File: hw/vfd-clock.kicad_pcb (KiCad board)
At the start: 2 copper layers, 150 x 50 mm, 47 parts, among them CON1 BARREL_JACK_2, CON2 BARREL_JACK_2, M1 MountingHole_4-5mm, M2 MountingHole_4-5mm, P1 ST_LINK, P2 GPS, Q1 PNP, Q2 PNP, SW1 SET, SW2 UP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

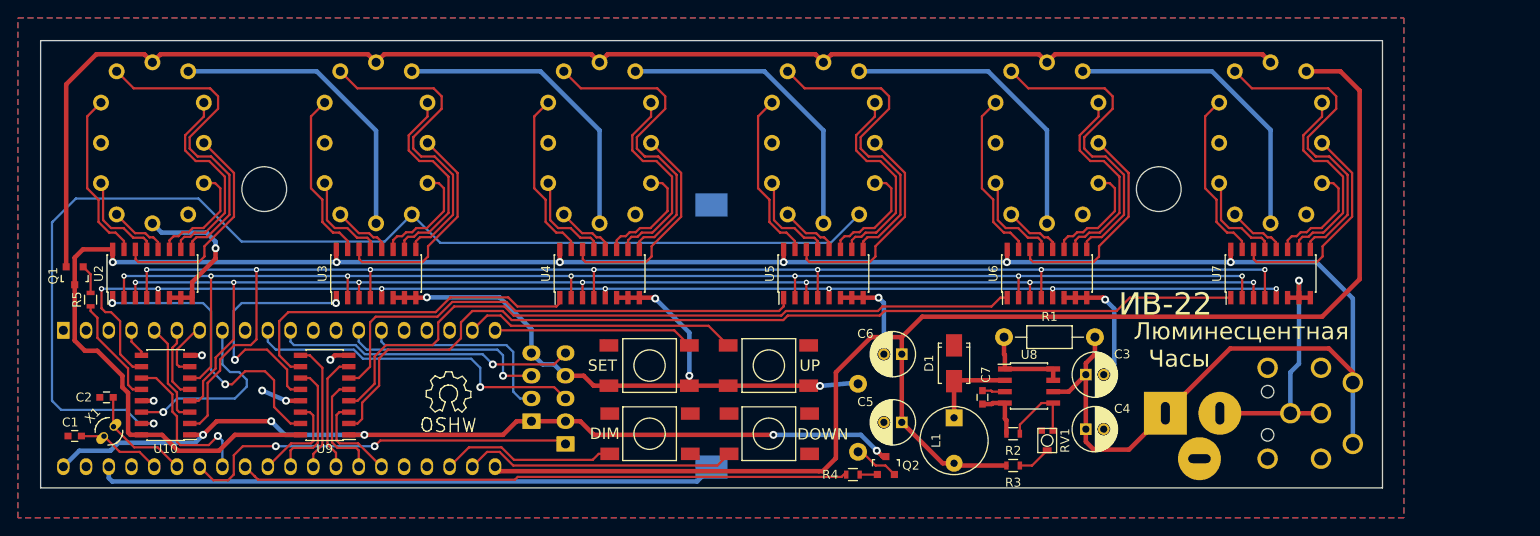
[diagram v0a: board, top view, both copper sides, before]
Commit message: fix transistor pin orientation
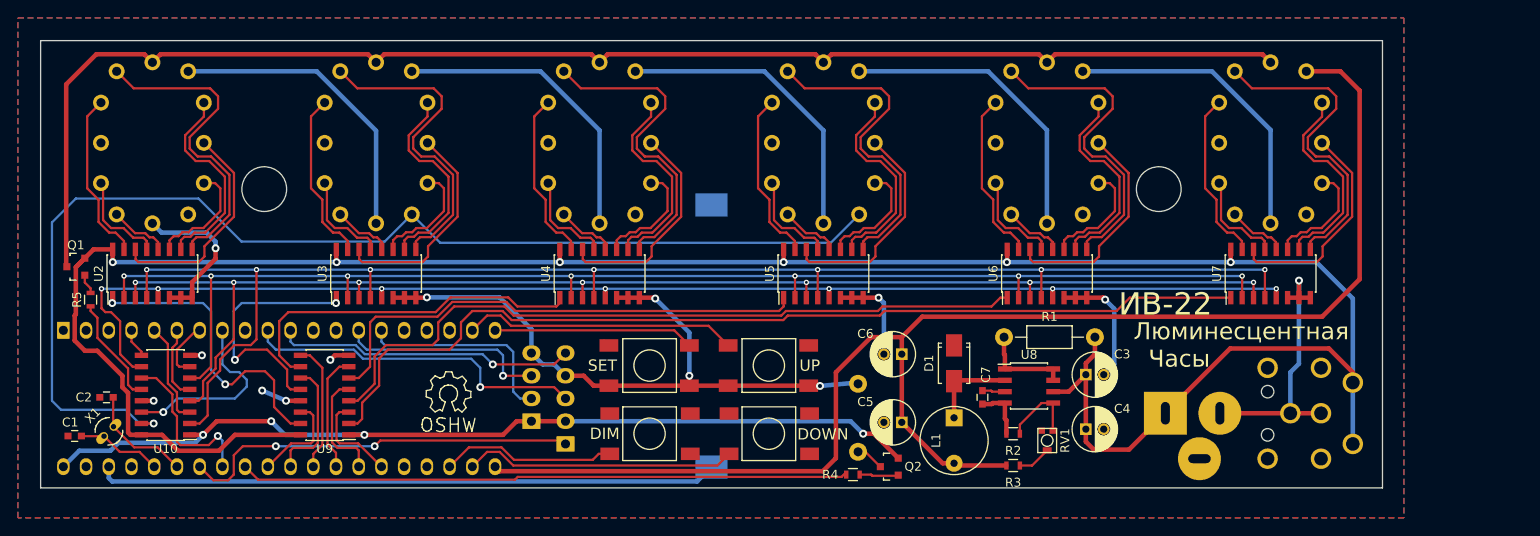
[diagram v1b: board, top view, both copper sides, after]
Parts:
- moved Q1 1.02 mm to (29.3, 50.7), turned to 90 degrees
- moved Q2 0.40 mm to (120.3, 73.0), turned to 90 degrees
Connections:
- Q1 pad 1: /GRID -> /19v5
- Q1 pad 3: /19v5 -> /GRID
- Q2 pad 1: Net-(Q2-Pad1) -> /3v3
- Q2 pad 3: /3v3 -> Net-(Q2-Pad3)
- SP1 pad 1: Net-(Q2-Pad1) -> Net-(Q2-Pad3)
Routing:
- net Net-(Q2-Pad1): track 5.04 -> 0.00 mm
- net Net-(Q2-Pad3): track 0.00 -> 3.18 mm
- net Net-(Q2-Pad2): track 1.99 -> 4.39 mm
- net /3v3: track 100.2 -> 101.6 mm, vias 5 -> 4
- net Net-(Q1-Pad2): track 3.26 -> 2.25 mm
- net /19v5: track 268.5 -> 269.3 mm

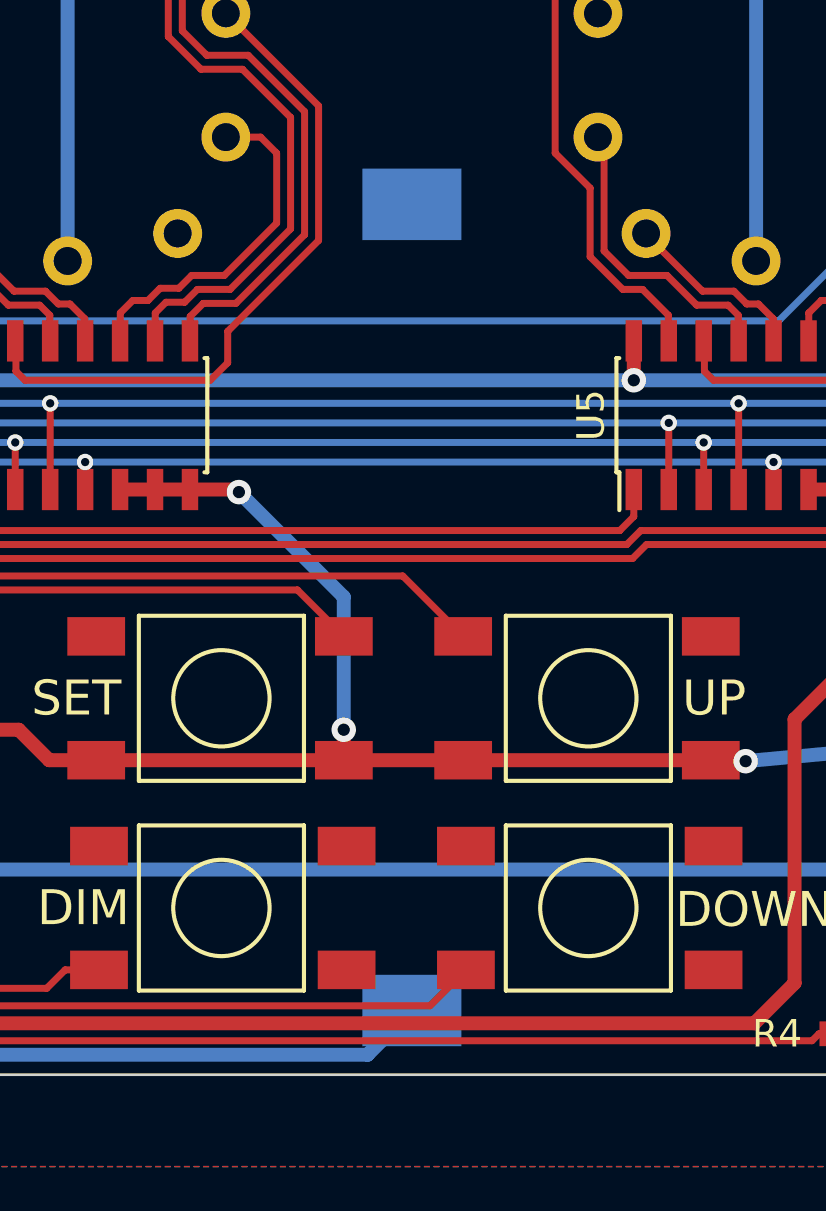
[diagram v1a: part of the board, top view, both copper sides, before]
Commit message: widen battery terminals for easier hand soldering
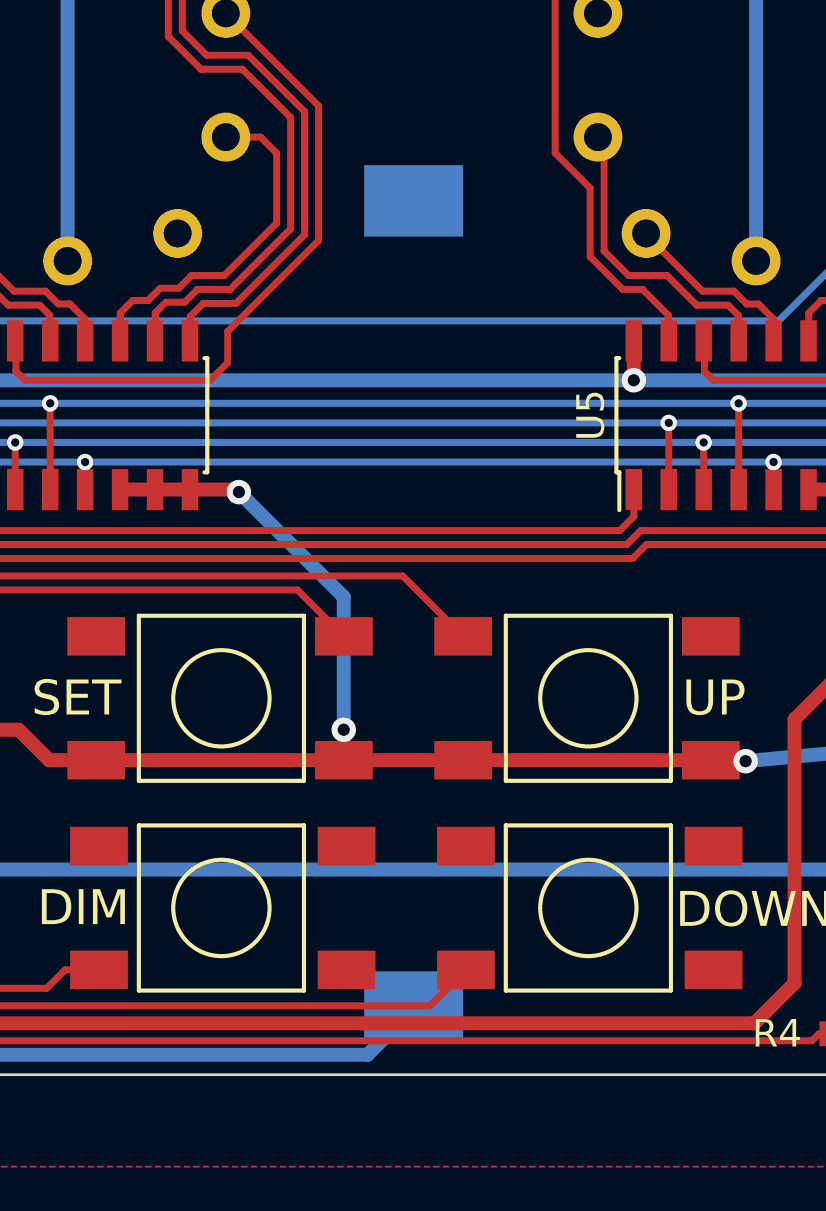
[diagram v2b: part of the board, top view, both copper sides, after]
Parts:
- moved BT1 0.14 mm to (100.5, 58.3)

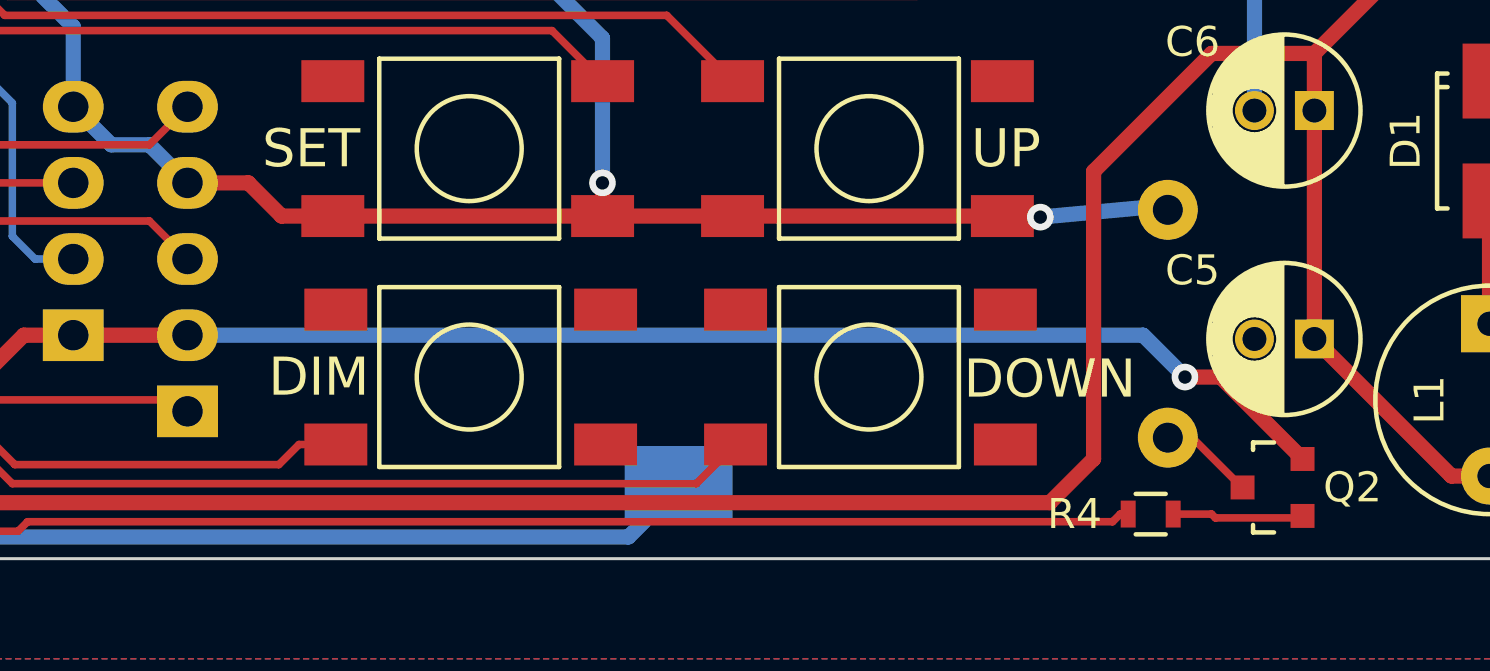
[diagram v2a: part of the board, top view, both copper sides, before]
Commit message: fix buzzer pin width
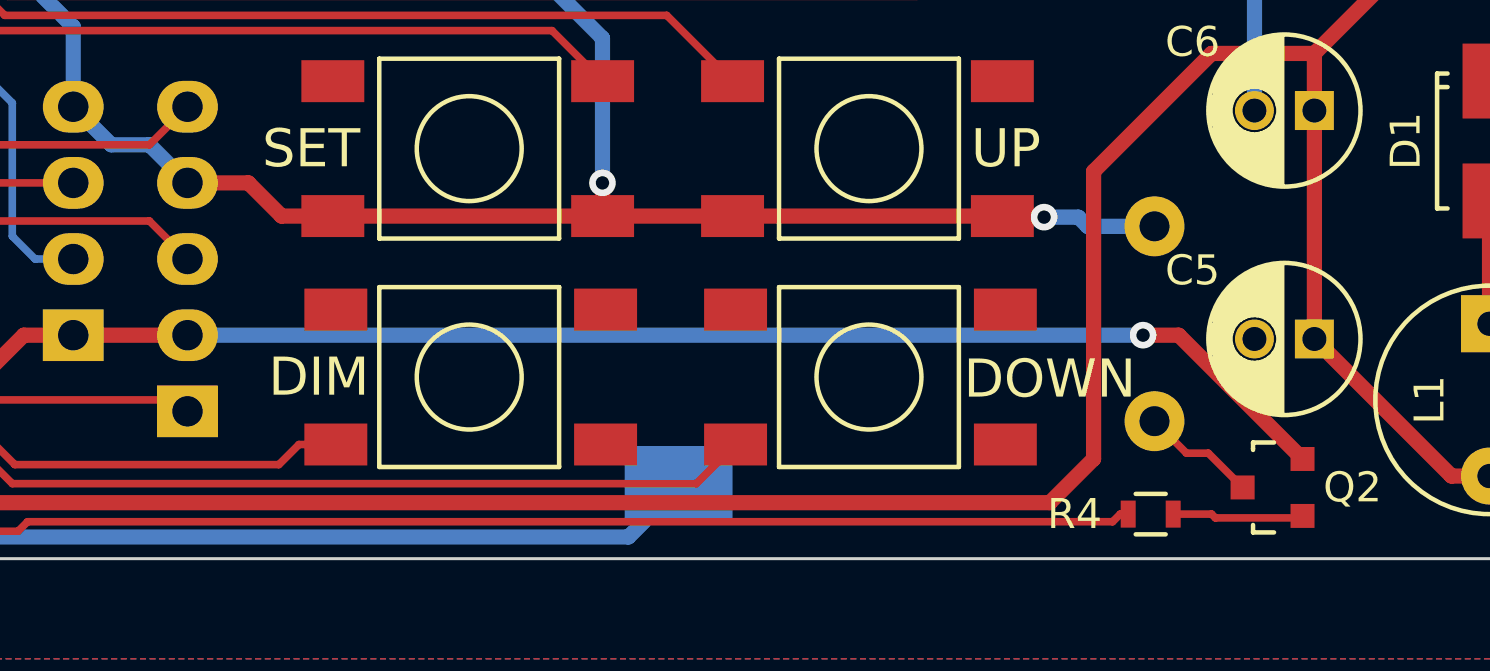
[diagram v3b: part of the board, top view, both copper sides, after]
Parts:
- SP1: footprint Buzzers_Beepers:Buzzer_12x9.5RM7.6 -> AT-1224-TWT
- moved SP1 0.44 mm to (116.3, 67.6)
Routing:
- net Net-(Q2-Pad3): track 3.18 -> 3.87 mm
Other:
- rule trace_min: 0.254 -> 0.01
- rule via_min_size: 0.381 -> 0.015
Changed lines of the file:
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@@
     (thickness 1.6)
     (drawings 11)
-    (tracks 1039)
+    (tracks 1041)
     (zones 0)
     (modules 47)
@@
     (zone_clearance 0.254)
     (zone_45_only no)
-    (trace_min 0.254)
+    (trace_min 0.01)
     (segment_width 0.2)
     (edge_width 0.1)
     (via_size 0.889)
     (via_drill 0.635)
-    (via_min_size 0.381)
+    (via_min_size 0.015)
     (via_min_drill 0.254)
     (uvia_size 0.508)
     (uvia_drill 0.127)
     (uvias_allowed yes)
-    (uvia_min_size 0.508)
+    (uvia_min_size 0.02)
     (uvia_min_drill 0.127)
     (pcb_text_width 0.3)
@@
     (add_net "Net-(D1-Pad2)")
   )
+  (module AT-1224-TWT (layer B.Cu)
+    (at 116.332 67.564 90)
+    (descr "Generic Buzzer, D12mm height 9.5mm with RM7.6mm")
+    (tags buzzer)
+    (fp_text reference SP1 (at 0 6.985 90) (layer B.SilkS)
+      (effects (font (size 1 1) (thickness 0.15)) (justify mirror))
+    )
+    (fp_text value SPEAKER (at 0 -8.255 90) (layer B.Fab)
+      (effects (font (size 1 1) (thickness 0.15)) (justify mirror))
+    )
+    (fp_text user + (at -3.175 2.54 90) (layer B.SilkS)
+      (effects (font (size 1 1) (thickness 0.15)) (justify mirror))
+    )
+    (fp_circle (center 0 0) (end 6 0) (layer B.SilkS) (width 0.15))
+    (pad 1 thru_hole circle (at -3.25 0 90) (size 2 2) (drill 1.00076) (layers *.Cu *.Mask B.SilkS)
+      (net 97 "Net-(Q2-Pad3)"))
+    (pad 2 thru_hole circle (at 3.25 0 90) (size 2 2) (drill 1.00076) (layers *.Cu *.Mask B.SilkS)
+      (net 1 /GND))
+    (model Buzzers_Beepers.3dshapes/Buzzer_12x9.5RM7.6.wrl
+      (at (xyz 0 0 0))
+      (scale (xyz 4 4 4))
+      (rotate (xyz 0 0 0))
+    )
+  )
   (module Diodes_SMD:Diode-SMA_Standard (layer F.Cu)
     (at 127.508 61.468 270)
@@
     )
   )
-  (module Buzzers_Beepers:Buzzer_12x9.5RM7.6 (layer B.Cu)
-    (at 116.7765 67.564 90)
-    (descr "Generic Buzzer, D12mm height 9.5mm with RM7.6mm")
-    (tags buzzer)
-    (fp_text reference SP1 (at 0 8.001 90) (layer B.SilkS)
-      (effects (font (size 1 1) (thickness 0.15)) (justify mirror))
-    )
-    (fp_text value SPEAKER (at -1.00076 -8.001 90) (layer B.Fab)
-      (effects (font (size 1 1) (thickness 0.15)) (justify mirror))
-    )
-    (fp_circle (center 0 0) (end 1.00076 0) (layer B.SilkS) (width 0.15))
-    (fp_text user + (at -3.81 2.54 90) (layer B.SilkS)
-      (effects (font (size 1 1) (thickness 0.15)) (justify mirror))
-    )
-    (fp_circle (center 0 0) (end 6.20014 0) (layer B.SilkS) (width 0.15))
-    (pad 1 thru_hole circle (at -3.79984 0 90) (size 2 2) (drill 1.00076) (layers *.Cu *.Mask B.SilkS)
-      (net 97 "Net-(Q2-Pad3)"))
-    (pad 2 thru_hole circle (at 3.79984 0 90) (size 2 2) (drill 1.00076) (layers *.Cu *.Mask B.SilkS)
-      (net 1 /GND))
-    (model Buzzers_Beepers.3dshapes/Buzzer_12x9.5RM7.6.wrl
-      (at (xyz 0 0 0))
-      (scale (xyz 4 4 4))
-      (rotate (xyz 0 0 0))
-    )
-  )
   (module Resistors_SMD:R_0603 (layer F.Cu)
     (at 116.205 73.914 180)
@@
   (gr_line (start 175.4 25.4) (end 175.4 75.4) (angle 90) (layer Edge.Cuts) (width 0.1))
   (gr_line (start 25.4 25.4) (end 175.4 25.4) (angle 90) (layer Edge.Cuts) (width 0.1))
+  (segment (start 116.7765 64.314) (end 114.098 64.314) (width 0.508) (layer B.Cu) (net 1) (status 10))
+  (segment (start 112.613 63.972) (end 111.257 63.972) (width 0.508) (layer F.Cu) (net 1) (status 20))
+  (segment (start 112.649 64.008) (end 112.613 63.972) (width 0.508) (layer F.Cu) (net 1))
+  (via (at 112.649 64.008) (size 0.889) (layers F.Cu B.Cu) (net 1))
+  (segment (start 113.792 64.008) (end 112.649 64.008) (width 0.508) (layer B.Cu) (net 1))
+  (segment (start 114.098 64.314) (end 113.792 64.008) (width 0.508) (layer B.Cu) (net 1))
   (segment (start 38.93058 46.863) (end 37.8968 45.82922) (width 0.508) (layer B.Cu) (net 1) (status 20))
   (segment (start 43.942 46.863) (end 38.93058 46.863) (width 0.508) (layer B.Cu) (net 1))
@@
   (segment (start 102.257 63.972) (end 97.922 63.972) (width 0.508) (layer F.Cu) (net 1) (status 30))
   (segment (start 111.257 63.972) (end 102.257 63.972) (width 0.508) (layer F.Cu) (net 1) (status 30))
-  (segment (start 116.7765 63.76416) (end 116.63934 63.627) (width 0.508) (layer B.Cu) (net 1) (status 30))
-  (segment (start 116.63934 63.627) (end 112.522 64.008) (width 0.508) (layer B.Cu) (net 1) (status 10))
-  (via (at 112.522 64.008) (size 0.889) (layers F.Cu B.Cu) (net 1))
-  (segment (start 112.522 64.008) (end 111.293 64.008) (width 0.508) (layer F.Cu) (net 1) (status 20))
   (segment (start 111.293 64.008) (end 111.257 63.972) (width 0.508) (layer F.Cu) (net 1) (status 30))
   (segment (start 84.074 62.865) (end 86.106 62.865) (width 0.508) (layer F.Cu) (net 1) (status 10))
@@
   (segment (start 114.3 72.0725) (end 114.3 62.484) (width 0.508) (layer F.Cu) (net 4))
   (segment (start 76.708002 73.533002) (end 112.839498 73.533002) (width 0.508) (layer F.Cu) (net 4) (status 10))
+  (segment (start 121.26976 72.075) (end 117.13976 67.945) (width 0.508) (layer F.Cu) (net 5) (status 10))
+  (segment (start 115.951 67.945) (end 84.074 67.945) (width 0.508) (layer B.Cu) (net 5) (status 20))
+  (via (at 115.951 67.945) (size 0.889) (layers F.Cu B.Cu) (net 5))
+  (segment (start 117.13976 67.945) (end 115.951 67.945) (width 0.508) (layer F.Cu) (net 5))
   (segment (start 80.264 67.945) (end 84.074 67.945) (width 0.508) (layer F.Cu) (net 5) (status 30))
   (segment (start 80.264 67.945) (end 78.613 67.945) (width 0.508) (layer F.Cu) (net 5) (status 10))
@@
   (segment (start 34.0995 70.358) (end 33.2105 71.247) (width 0.508) (layer B.Cu) (net 5))
   (segment (start 42.672 70.358) (end 34.0995 70.358) (width 0.508) (layer B.Cu) (net 5))
-  (segment (start 115.951 67.945) (end 117.348 69.342) (width 0.508) (layer B.Cu) (net 5))
-  (via (at 117.348 69.342) (size 0.889) (layers F.Cu B.Cu) (net 5))
-  (segment (start 117.348 69.342) (end 118.53676 69.342) (width 0.508) (layer F.Cu) (net 5))
-  (segment (start 118.53676 69.342) (end 121.26976 72.075) (width 0.508) (layer F.Cu) (net 5))
-  (segment (start 84.074 67.945) (end 115.951 67.945) (width 0.508) (layer B.Cu) (net 5))
   (segment (start 50.8 57.785) (end 50.8 59.055) (width 0.254) (layer B.Cu) (net 6) (status 10))
   (segment (start 82.804 64.135) (end 84.074 65.405) (width 0.254) (layer F.Cu) (net 6) (status 20))
@@
   (segment (start 30.33776 52.43576) (end 30.33776 51.623) (width 0.254) (layer F.Cu) (net 49) (status 20))
   (segment (start 30.988 53.606) (end 30.988 53.086) (width 0.254) (layer F.Cu) (net 49) (status 10))
-  (segment (start 121.20376 74.041) (end 121.26976 73.975) (width 0.254) (layer F.Cu) (net 50))
+  (segment (start 121.20376 74.041) (end 121.26976 73.975) (width 0.254) (layer F.Cu) (net 50) (status 30))
   (segment (start 118.237 73.914) (end 118.364 74.041) (width 0.254) (layer F.Cu) (net 50))
-  (segment (start 118.364 74.041) (end 121.20376 74.041) (width 0.254) (layer F.Cu) (net 50))
-  (segment (start 116.955 73.914) (end 118.237 73.914) (width 0.254) (layer F.Cu) (net 50))
+  (segment (start 118.364 74.041) (end 121.20376 74.041) (width 0.254) (layer F.Cu) (net 50) (status 20))
+  (segment (start 116.955 73.914) (end 118.237 73.914) (width 0.254) (layer F.Cu) (net 50) (status 10))
   (segment (start 63.5 57.785) (end 63.5 59.055) (width 0.254) (layer B.Cu) (net 51) (status 10))
   (segment (start 78.994 65.405) (end 80.264 65.405) (width 0.254) (layer B.Cu) (net 51) (status 20))
@@
   (segment (start 66.89598 44.82846) (end 63.86322 47.86122) (width 0.254) (layer B.Cu) (net 96) (status 10))
   (segment (start 27.686 66.675) (end 26.67 65.659) (width 0.254) (layer B.Cu) (net 96))
-  (segment (start 117.59184 71.36384) (end 116.7765 71.36384) (width 0.254) (layer F.Cu) (net 97))
-  (segment (start 119.253 73.025) (end 117.59184 71.36384) (width 0.254) (layer F.Cu) (net 97))
-  (segment (start 119.27078 73.025) (end 119.253 73.025) (width 0.254) (layer F.Cu) (net 97))
+  (segment (start 119.27078 73.025) (end 118.12778 71.882) (width 0.254) (layer F.Cu) (net 97) (status 10))
+  (segment (start 117.4 71.882) (end 116.332 70.814) (width 0.254) (layer F.Cu) (net 97) (status 20))
+  (segment (start 118.12778 71.882) (end 117.4 71.882) (width 0.254) (layer F.Cu) (net 97))
+  (segment (start 119.27078 73.025) (end 119.253 73.025) (width 0.254) (layer F.Cu) (net 97) (status 30))
   (zone (net 1) (net_name /GND) (layer B.Cu) (hatch edge 0.508)
     (connect_pads (clearance 0.254))
